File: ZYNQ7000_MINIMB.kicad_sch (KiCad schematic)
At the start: 34 parts, among them J1 Conn_02x50_Odd_Even, J10 Conn_02x20_Odd_Even, J12 Conn_01x40, J2 Conn_02x50_Odd_Even, J3 ZYNQ_JTAG, SW2 SW_DIP_x01, SW5 SW_DIP_x02, U1 HR911130A

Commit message: update layout
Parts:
- removed SYM1: SYM_Arrow45_Large, zynq7000_mb:LOGO, symbol Graphic:SYM_Arrow45_Large
- added RN1, RN2, RN3, RN4, RN5, RN6, RN7, RN8: R_Pack04, Resistor_SMD:R_Array_Concave_4x0603, symbol Device:R_Pack04
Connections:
- net B13_L11N: now also RN4.2 (R2.1); no longer J10.28 (Pin_28)
- net B13_L11P: now also RN3.7 (R2.2); no longer J10.27 (Pin_27)
- net B13_L13N: now also RN2.1 (R1.1); no longer J10.38 (Pin_38)
- net B13_L13P: now also RN1.8 (R1.2); no longer J10.37 (Pin_37)
- net B13_L14N: now also RN2.2 (R2.1); no longer J10.36 (Pin_36)
- net B13_L14P: now also RN1.7 (R2.2); no longer J10.35 (Pin_35)
- net B13_L16N: now also RN2.3 (R3.1); no longer J10.34 (Pin_34)
- net B13_L16P: now also RN1.6 (R3.2); no longer J10.33 (Pin_33)
- net B13_L18N: now also RN2.4 (R4.1); no longer J10.32 (Pin_32)
- net B13_L18P: now also RN1.5 (R4.2); no longer J10.31 (Pin_31)
- net B13_L19N: now also RN4.1 (R1.1); no longer J10.30 (Pin_30)
- net B13_L19P: now also RN3.8 (R1.2); no longer J10.29 (Pin_29)
- net B34_L10N: now also RN6.3 (R3.1); no longer J10.16 (Pin_16)
- net B34_L10P: now also RN5.6 (R3.2); no longer J10.15 (Pin_15)
- net B34_L1N: now also RN4.3 (R3.1); no longer J10.24 (Pin_24)
- net B34_L1P: now also RN3.6 (R3.2); no longer J10.23 (Pin_23)
- net B34_L2N: now also RN4.4 (R4.1); no longer J10.22 (Pin_22)
- net B34_L2P: now also RN3.5 (R4.2); no longer J10.21 (Pin_21)
- net B34_L7N: now also RN6.4 (R4.1); no longer J10.14 (Pin_14)
- net B34_L7P: now also RN5.5 (R4.2); no longer J10.13 (Pin_13)
- net B34_L8N: now also RN6.2 (R2.1); no longer J10.18 (Pin_18)
- net B34_L8P: now also RN5.7 (R2.2); no longer J10.17 (Pin_17)
- net B34_L9N: now also RN6.1 (R1.1); no longer J10.20 (Pin_20)
- net B34_L9P: now also RN5.8 (R1.2); no longer J10.19 (Pin_19)
- net B35_L11N: now also RN8.4 (R4.1); no longer J10.4 (Pin_4)
- net B35_L11P: now also RN7.5 (R4.2); no longer J10.3 (Pin_3)
- net B35_L21N: now also RN8.3 (R3.1); no longer J10.6 (Pin_6)
- net B35_L21P: now also RN7.6 (R3.2); no longer J10.5 (Pin_5)
- net B35_L7N: now also RN8.1 (R1.1); no longer J10.10 (Pin_10)
- net B35_L7P: now also RN7.8 (R1.2); no longer J10.9 (Pin_9)
- net B35_L9N: now also RN8.2 (R2.1); no longer J10.8 (Pin_8)
- net B35_L9P: now also RN7.7 (R2.2); no longer J10.7 (Pin_7)
- new net: J10.19 (Pin_19), RN5.1 (R1.1)
- new net: J10.17 (Pin_17), RN5.2 (R2.1)
- new net: J10.15 (Pin_15), RN5.3 (R3.1)
- new net: J10.13 (Pin_13), RN5.4 (R4.1)
- new net: J10.32 (Pin_32), RN2.5 (R4.2)
- new net: J10.34 (Pin_34), RN2.6 (R3.2)
- new net: J10.36 (Pin_36), RN2.7 (R2.2)
- new net: J10.38 (Pin_38), RN2.8 (R1.2)
- new net: J10.10 (Pin_10), RN8.8 (R1.2)
- new net: J10.14 (Pin_14), RN6.5 (R4.2)
- new net: J10.16 (Pin_16), RN6.6 (R3.2)
- new net: J10.18 (Pin_18), RN6.7 (R2.2)
- new net: J10.20 (Pin_20), RN6.8 (R1.2)
- new net: J10.21 (Pin_21), RN3.4 (R4.1)
- new net: J10.22 (Pin_22), RN4.5 (R4.2)
- new net: J10.23 (Pin_23), RN3.3 (R3.1)
- new net: J10.24 (Pin_24), RN4.6 (R3.2)
- new net: J10.27 (Pin_27), RN3.2 (R2.1)
- new net: J10.28 (Pin_28), RN4.7 (R2.2)
- new net: J10.29 (Pin_29), RN3.1 (R1.1)
- new net: J10.3 (Pin_3), RN7.4 (R4.1)
- new net: J10.30 (Pin_30), RN4.8 (R1.2)
- new net: J10.31 (Pin_31), RN1.4 (R4.1)
- new net: J10.33 (Pin_33), RN1.3 (R3.1)
- new net: J10.35 (Pin_35), RN1.2 (R2.1)
- new net: J10.37 (Pin_37), RN1.1 (R1.1)
- new net: J10.4 (Pin_4), RN8.5 (R4.2)
- new net: J10.5 (Pin_5), RN7.3 (R3.1)
- new net: J10.6 (Pin_6), RN8.6 (R3.2)
- new net: J10.7 (Pin_7), RN7.2 (R2.1)
- new net: J10.8 (Pin_8), RN8.7 (R2.2)
- new net: J10.9 (Pin_9), RN7.1 (R1.1)
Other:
- moved on the sheet: J10

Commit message: update sch&layout
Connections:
- net B13_L11N: no longer RN4.2 (R2.1)
- net B13_L11P: no longer RN3.7 (R2.2)
- net B13_L12N: now also J12.35 (Pin_35)
- net B13_L12P: now also J12.34 (Pin_34)
- net B13_L13N: now also RN1.5 (R4.2); no longer RN2.1 (R1.1)
- net B13_L13P: now also RN1.6 (R3.2); no longer RN1.8 (R1.2)
- net B13_L14N: now also RN1.7 (R2.2); no longer RN2.2 (R2.1)
- net B13_L14P: now also RN1.8 (R1.2); no longer RN1.7 (R2.2)
- net B13_L16N: no longer RN2.3 (R3.1)
- net B13_L16P: no longer RN1.6 (R3.2)
- net B13_L18N: now also RN2.5 (R4.2); no longer RN2.4 (R4.1)
- net B13_L18P: now also RN2.6 (R3.2); no longer RN1.5 (R4.2)
- net B13_L19N: now also RN2.7 (R2.2); no longer RN4.1 (R1.1)
- net B13_L19P: now also RN2.8 (R1.2); no longer RN3.8 (R1.2)
- net B13_L20N: now also J12.37 (Pin_37)
- net B13_L20P: now also J12.36 (Pin_36)
- net B13_L21N: now also J12.39 (Pin_39)
- net B13_L21P: now also J12.38 (Pin_38)
- net B34_IO25: now also RN8.5 (R4.2)
- net B34_L10N: now also RN3.7 (R2.2); no longer RN6.3 (R3.1)
- net B34_L10P: now also RN3.8 (R1.2); no longer RN5.6 (R3.2)
- net B34_L11N: now also J12.27 (Pin_27)
- net B34_L11P: now also J12.26 (Pin_26)
- net B34_L12N: now also RN8.6 (R3.2)
- net B34_L13N: now also J12.13 (Pin_13)
- net B34_L13P: now also J12.12 (Pin_12)
- net B34_L14N: now also J12.11 (Pin_11)
- net B34_L14P: now also J12.10 (Pin_10)
- net B34_L15N: now also RN6.7 (R2.2)
- net B34_L15P: now also RN6.8 (R1.2)
- net B34_L16N: now also RN5.7 (R2.2)
- net B34_L16P: now also RN5.8 (R1.2)
- net B34_L17N: now also RN5.5 (R4.2)
- net B34_L17P: now also RN5.6 (R3.2)
- net B34_L18N: now also J12.23 (Pin_23)
- net B34_L18P: now also J12.22 (Pin_22)
- net B34_L1N: now also RN4.5 (R4.2); no longer RN4.3 (R3.1)
- net B34_L1P: now also RN4.6 (R3.2); no longer RN3.6 (R3.2)
- net B34_L20N: now also J12.19 (Pin_19)
- net B34_L20P: now also J12.18 (Pin_18)
- net B34_L21N: now also J12.25 (Pin_25)
- net B34_L21P: now also J12.24 (Pin_24)
- net B34_L22N: now also J12.21 (Pin_21)
- net B34_L22P: now also J12.20 (Pin_20)
- net B34_L23N: now also J12.15 (Pin_15)
- net B34_L23P: now also J12.14 (Pin_14)
- net B34_L24N: now also RN6.5 (R4.2)
- net B34_L24P: now also RN6.6 (R3.2)
- net B34_L2N: now also RN4.7 (R2.2); no longer RN4.4 (R4.1)
- net B34_L2P: now also RN4.8 (R1.2); no longer RN3.5 (R4.2)
- net B34_L3N: now also J12.31 (Pin_31)
- net B34_L3P: now also J12.30 (Pin_30)
- net B34_L4N: now also J12.33 (Pin_33)
- net B34_L4P: now also J12.32 (Pin_32)
- net B34_L5N: now also J12.29 (Pin_29)
- net B34_L5P: now also J12.28 (Pin_28)
- net B34_L6N: now also J12.17 (Pin_17)
- net B34_L6P: now also J12.16 (Pin_16)
- net B34_L7N: no longer RN6.4 (R4.1)
- net B34_L7P: no longer RN5.5 (R4.2)
- net B34_L8N: now also RN3.5 (R4.2); no longer RN6.2 (R2.1)
- net B34_L8P: now also RN3.6 (R3.2); no longer RN5.7 (R2.2)
- net B34_L9N: no longer RN6.1 (R1.1)
- net B34_L9P: no longer RN5.8 (R1.2)
- net B35_L11N: now also RN7.7 (R2.2); no longer RN8.4 (R4.1)
- net B35_L11P: now also RN7.8 (R1.2); no longer RN7.5 (R4.2)
- net B35_L12N: now also J12.7 (Pin_7)
- net B35_L12P: now also J12.6 (Pin_6)
- net B35_L17N: now also J12.3 (Pin_3)
- net B35_L17P: now also J12.2 (Pin_2)
- net B35_L21N: now also RN7.5 (R4.2); no longer RN8.3 (R3.1)
- net B35_L23N: now also J12.5 (Pin_5)
- net B35_L23P: now also J12.4 (Pin_4)
- net B35_L7N: now also RN8.7 (R2.2); no longer RN8.1 (R1.1)
- net B35_L7P: now also RN8.8 (R1.2); no longer RN7.8 (R1.2)
- net B35_L8N: now also J12.9 (Pin_9)
- net B35_L8P: now also J12.8 (Pin_8)
- net B35_L9N: no longer RN8.2 (R2.1)
- net B35_L9P: no longer RN7.7 (R2.2)
- net GND: now also J12.40 (Pin_40); no longer J10.25 (Pin_25), J10.26 (Pin_26)
- net VDD5VD: now also J12.1 (Pin_1)
- net P17: now reaches RN5.1 (R1.1)
- net P17: now also J10.17 (Pin_17); no longer J10.19 (Pin_19)
- net P18: now reaches RN5.2 (R2.1)
- net P18: now also J10.18 (Pin_18); no longer J10.17 (Pin_17)
- net P15: now reaches J10.15 (Pin_15)
- net P15: now also RN6.3 (R3.1); no longer RN5.3 (R3.1)
- net P13: now reaches J10.13 (Pin_13)
- net P13: now also RN6.1 (R1.1); no longer RN5.4 (R4.1)
- net P32: now reaches J10.32 (Pin_32)
- net P32: now also RN2.4 (R4.1); no longer RN2.5 (R4.2)
- net P34: now reaches J10.34 (Pin_34)
- net P34: now also RN1.2 (R2.1); no longer RN2.6 (R3.2)
- net P36: now reaches J10.36 (Pin_36)
- net P36: now also RN1.4 (R4.1); no longer RN2.7 (R2.2)
- net at J10.38 (Pin_38): no longer RN2.8 (R1.2)
- net P10: now reaches J10.10 (Pin_10)
- net P10: now also RN8.4 (R4.1); no longer RN8.8 (R1.2)
- net P14: now reaches J10.14 (Pin_14)
- net P14: now also RN6.2 (R2.1); no longer RN6.5 (R4.2)
- net P16: now reaches J10.16 (Pin_16)
- net P16: now also RN6.4 (R4.1); no longer RN6.6 (R3.2)
- net P20: now reaches J10.20 (Pin_20)
- net P20: now also RN5.4 (R4.1); no longer RN6.8 (R1.2)
- net P21: now reaches J10.21 (Pin_21)
- net P21: now also RN3.1 (R1.1); no longer RN3.4 (R4.1)
- net P22: now reaches J10.22 (Pin_22)
- net P22: now also RN3.2 (R2.1); no longer RN4.5 (R4.2)
- net P23: now reaches J10.23 (Pin_23), RN3.3 (R3.1)
- net P24: now reaches J10.24 (Pin_24)
- net P24: now also RN3.4 (R4.1); no longer RN4.6 (R3.2)
- net P27: now reaches J10.27 (Pin_27)
- net P27: now also RN4.3 (R3.1); no longer RN3.2 (R2.1)
- net P28: now reaches J10.28 (Pin_28)
- net P28: now also RN4.4 (R4.1); no longer RN4.7 (R2.2)
- net P29: now reaches J10.29 (Pin_29)
- net P29: now also RN2.1 (R1.1); no longer RN3.1 (R1.1)
- net P3: now reaches J10.3 (Pin_3)
- net P3: now also RN7.1 (R1.1); no longer RN7.4 (R4.1)
- net P30: now reaches J10.30 (Pin_30)
- net P30: now also RN2.2 (R2.1); no longer RN4.8 (R1.2)
- net P31: now reaches J10.31 (Pin_31)
- net P31: now also RN2.3 (R3.1); no longer RN1.4 (R4.1)
- net P33: now reaches J10.33 (Pin_33)
- net P33: now also RN1.1 (R1.1); no longer RN1.3 (R3.1)
- net P35: now reaches J10.35 (Pin_35)
- net P35: now also RN1.3 (R3.1); no longer RN1.2 (R2.1)
- net at J10.37 (Pin_37): no longer RN1.1 (R1.1)
- net P4: now reaches J10.4 (Pin_4)
- net P4: now also RN7.2 (R2.1); no longer RN8.5 (R4.2)
- net P5: now reaches J10.5 (Pin_5), RN7.3 (R3.1)
- net P6: now reaches J10.6 (Pin_6)
- net P6: now also RN7.4 (R4.1); no longer RN8.6 (R3.2)
- net P7: now reaches J10.7 (Pin_7)
- net P7: now also RN8.1 (R1.1); no longer RN7.2 (R2.1)
- net P8: now reaches J10.8 (Pin_8)
- net P8: now also RN8.2 (R2.1); no longer RN8.7 (R2.2)
- net P9: now reaches J10.9 (Pin_9)
- net P9: now also RN8.3 (R3.1); no longer RN7.1 (R1.1)
- new net P19: J10.19 (Pin_19), RN5.3 (R3.1)
- new net P25: J10.25 (Pin_25), RN4.1 (R1.1)
- new net P26: J10.26 (Pin_26), RN4.2 (R2.1)
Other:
- moved on the sheet: J10, J12, RN1, RN2, RN3, RN4, RN5, RN6, RN7, RN8

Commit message: update sch&layout
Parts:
- removed J12: Conn_01x40, Connector_FFC-FPC:Hirose_FH12-40S-0.5SH_1x40-1MP_P0.50mm_Horizontal, symbol Connector_Generic:Conn_01x40
- added J12: Conn_01x30, Connector_FFC-FPC:Hirose_FH12-30S-0.5SH_1x30-1MP_P0.50mm_Horizontal, symbol Connector_Generic:Conn_01x30
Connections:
- net B0MIO11: now also J12.26 (Pin_26)
- net B0MIO12: now also J12.27 (Pin_27)
- net B0MIO13: now also J12.28 (Pin_28)
- net B13_L06N: now also J12.14 (Pin_14)
- net B13_L12N: now also J12.15 (Pin_15)
- net B13_L12P: now also J12.16 (Pin_16)
- net B13_L15N: now also J12.10 (Pin_10)
- net B13_L15P: now also J12.9 (Pin_9)
- net B13_L17N: now also J12.8 (Pin_8)
- net B13_L17P: now also J12.7 (Pin_7)
- net B13_L20N: now also J12.4 (Pin_4)
- net B13_L20P: now also J12.3 (Pin_3)
- net B13_L21N: now also J12.6 (Pin_6)
- net B13_L21P: now also J12.5 (Pin_5)
- net B13_L22N: now also J12.12 (Pin_12)
- net B13_L22P: now also J12.11 (Pin_11)
- net B34_L11N: now also J12.23 (Pin_23)
- net B34_L11P: now also J12.24 (Pin_24)
- net B34_L3N: now also J12.19 (Pin_19)
- net B34_L3P: now also J12.20 (Pin_20)
- net B34_L4N: now also J12.17 (Pin_17)
- net B34_L4P: now also J12.18 (Pin_18)
- net B34_L5N: now also J12.21 (Pin_21)
- net B34_L5P: now also J12.22 (Pin_22)
- net GND: now also J12.13 (Pin_13), J12.25 (Pin_25), J12.29 (Pin_29), J12.30 (Pin_30)
- net VDD5VD: now also J12.1 (Pin_1), J12.2 (Pin_2)

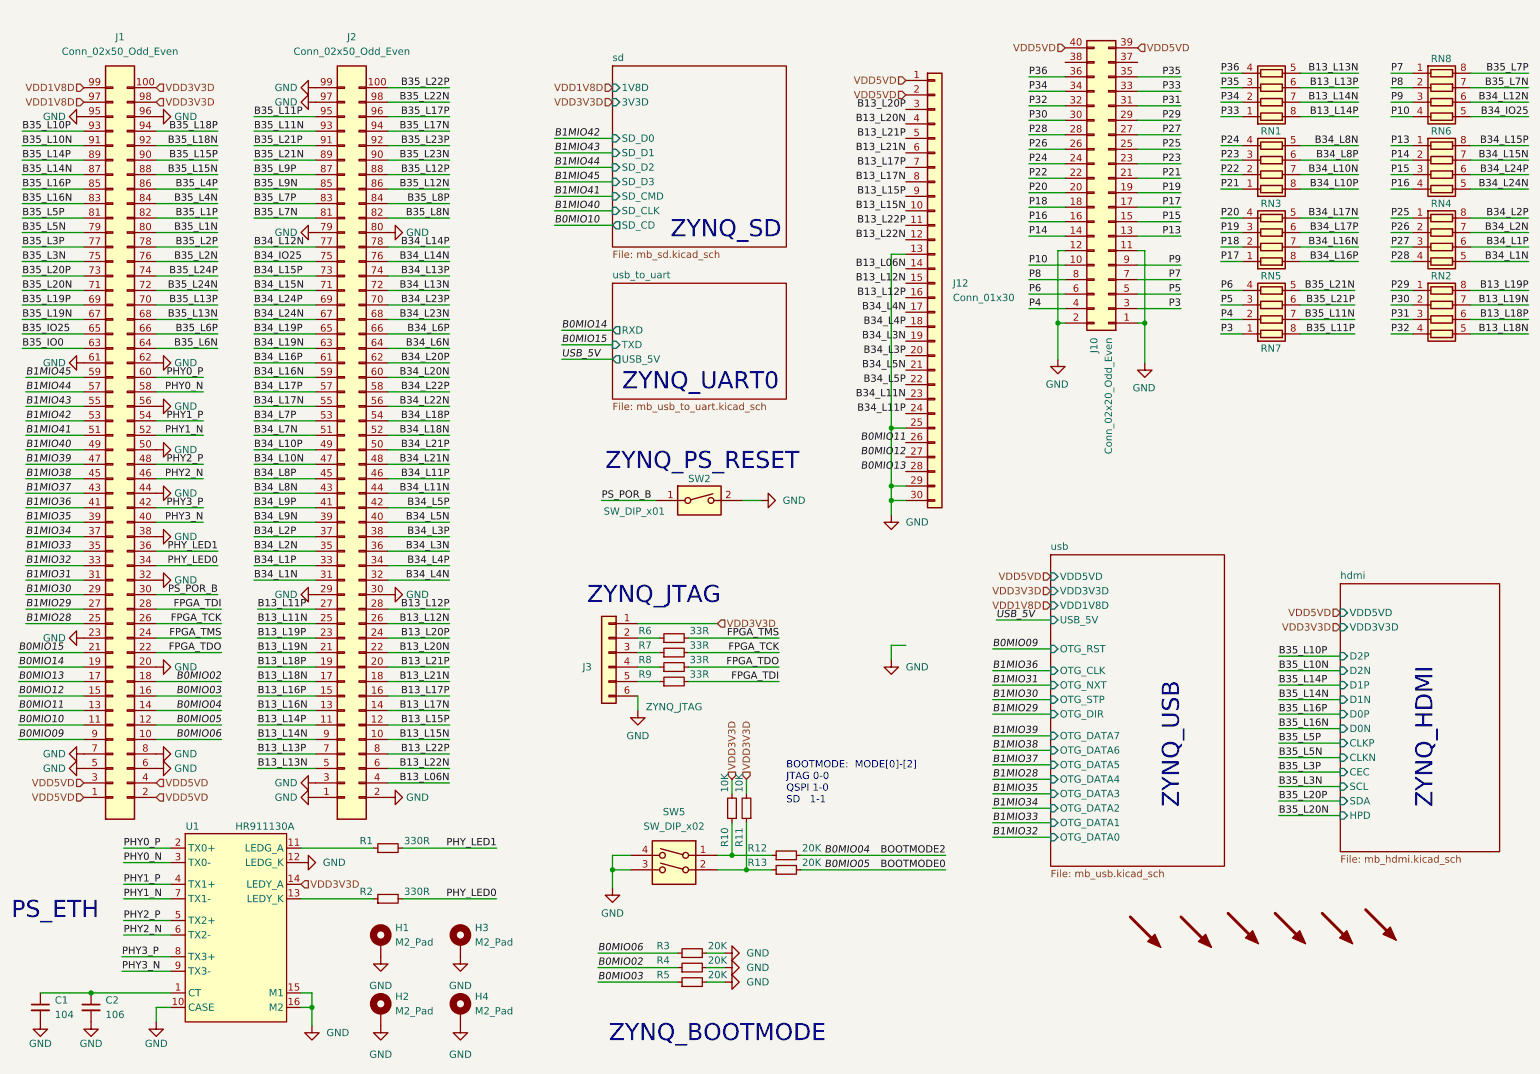
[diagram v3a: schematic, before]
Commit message: length matching
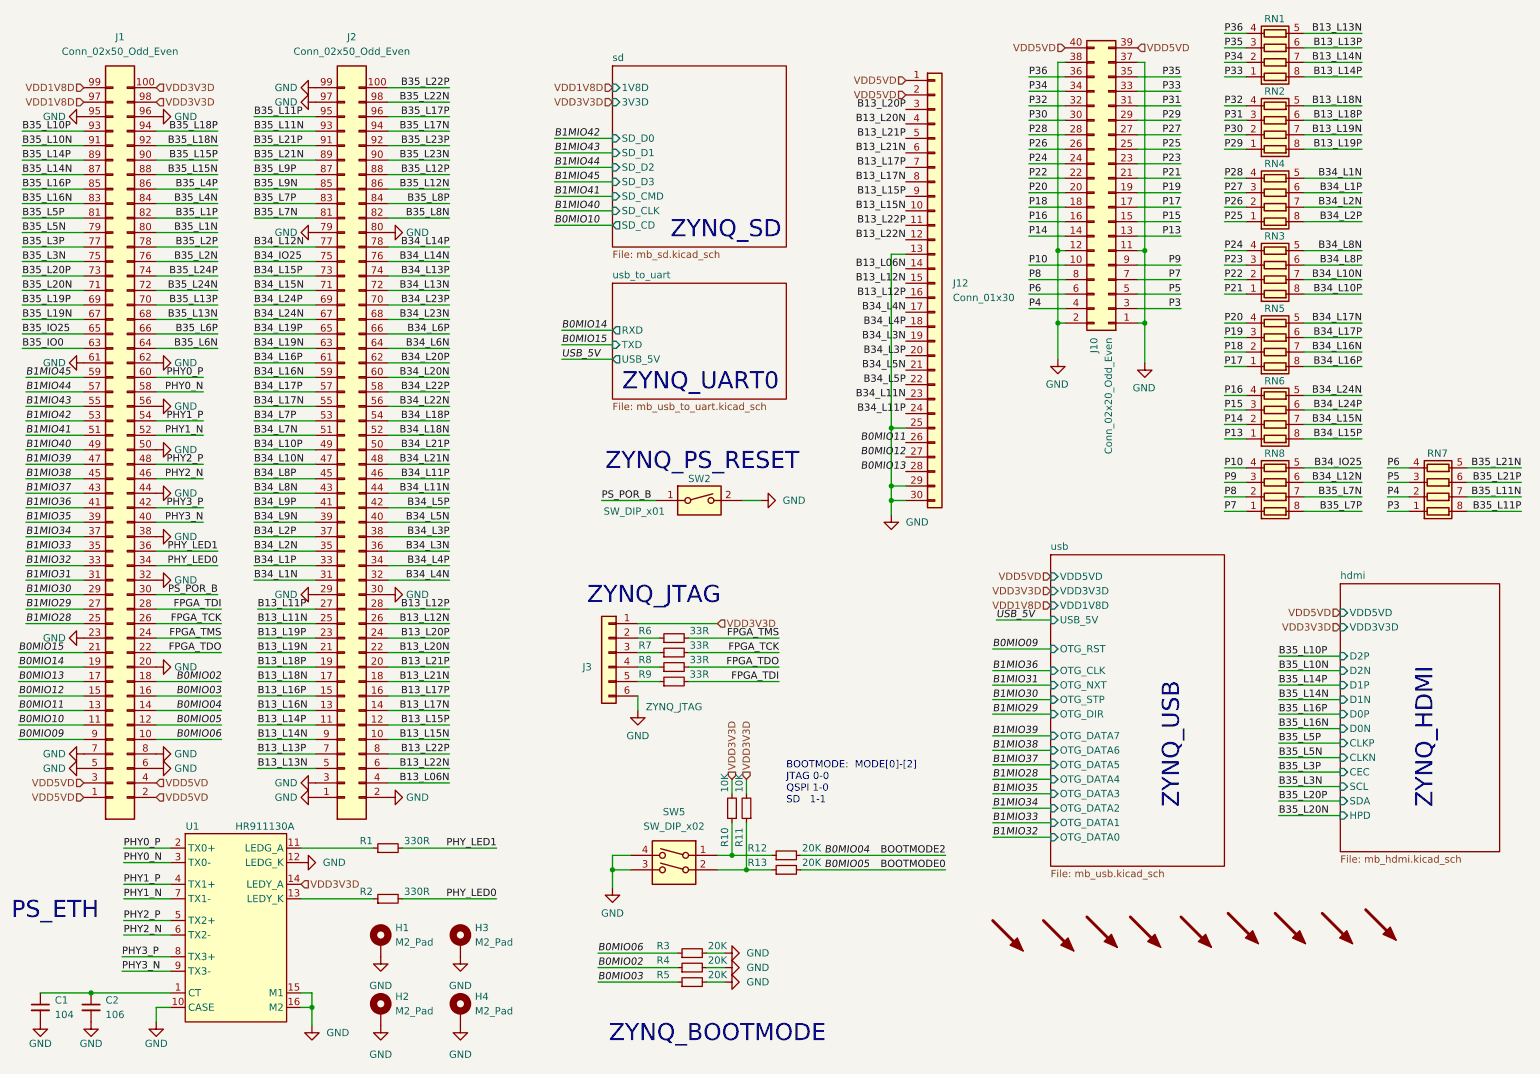
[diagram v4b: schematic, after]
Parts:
- added SYME7: SYM_Arrow45_Large, Symbol:FCC-Logo_7.3x6mm_SilkScreen, symbol Graphic:SYM_Arrow45_Large
- added SYME8: SYM_Arrow45_Large, Symbol:OSHW-Logo2_9.8x8mm_SilkScreen, symbol Graphic:SYM_Arrow45_Large
- added SYME9: SYM_Arrow45_Large, Symbol:CE-Logo_8.5x6mm_SilkScreen, symbol Graphic:SYM_Arrow45_Large
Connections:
- net GND: now also J10.37 (Pin_37), J10.38 (Pin_38)
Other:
- moved on the sheet: RN1, RN2, RN3, RN4, RN5, RN6, RN7, RN8

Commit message: finall version
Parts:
- added SYME10: SYM_Arrow45_Large, zynq7000_mb:LOGO_Arrow, symbol Graphic:SYM_Arrow45_Large
